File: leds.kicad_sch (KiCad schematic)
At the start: 123 parts, among them U14 ADUM1201ARZ-RL7

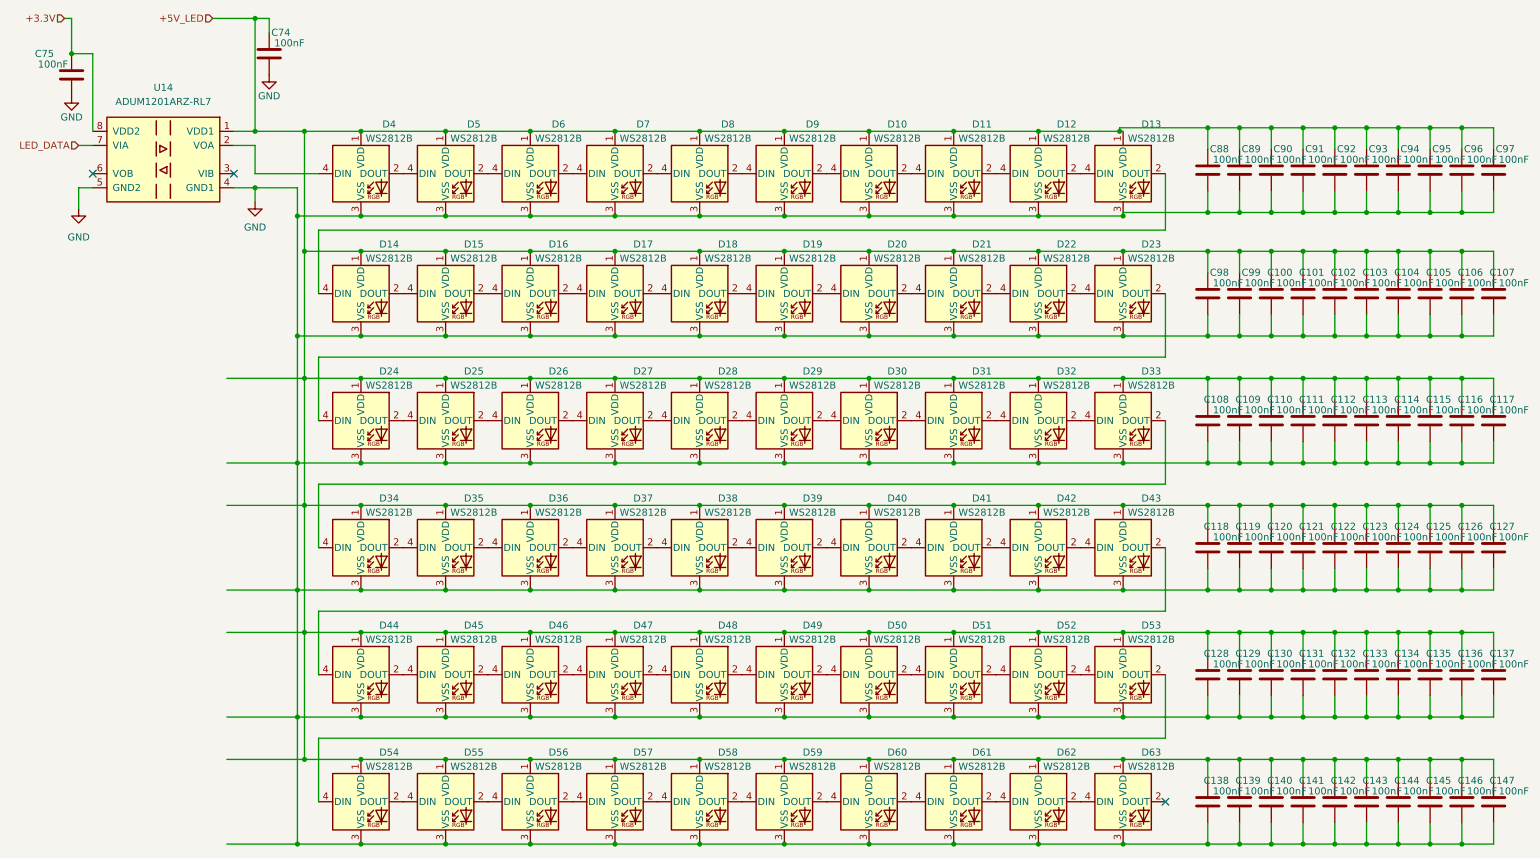
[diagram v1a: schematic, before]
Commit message: updated to kicad 9, added comparator-based power source switching
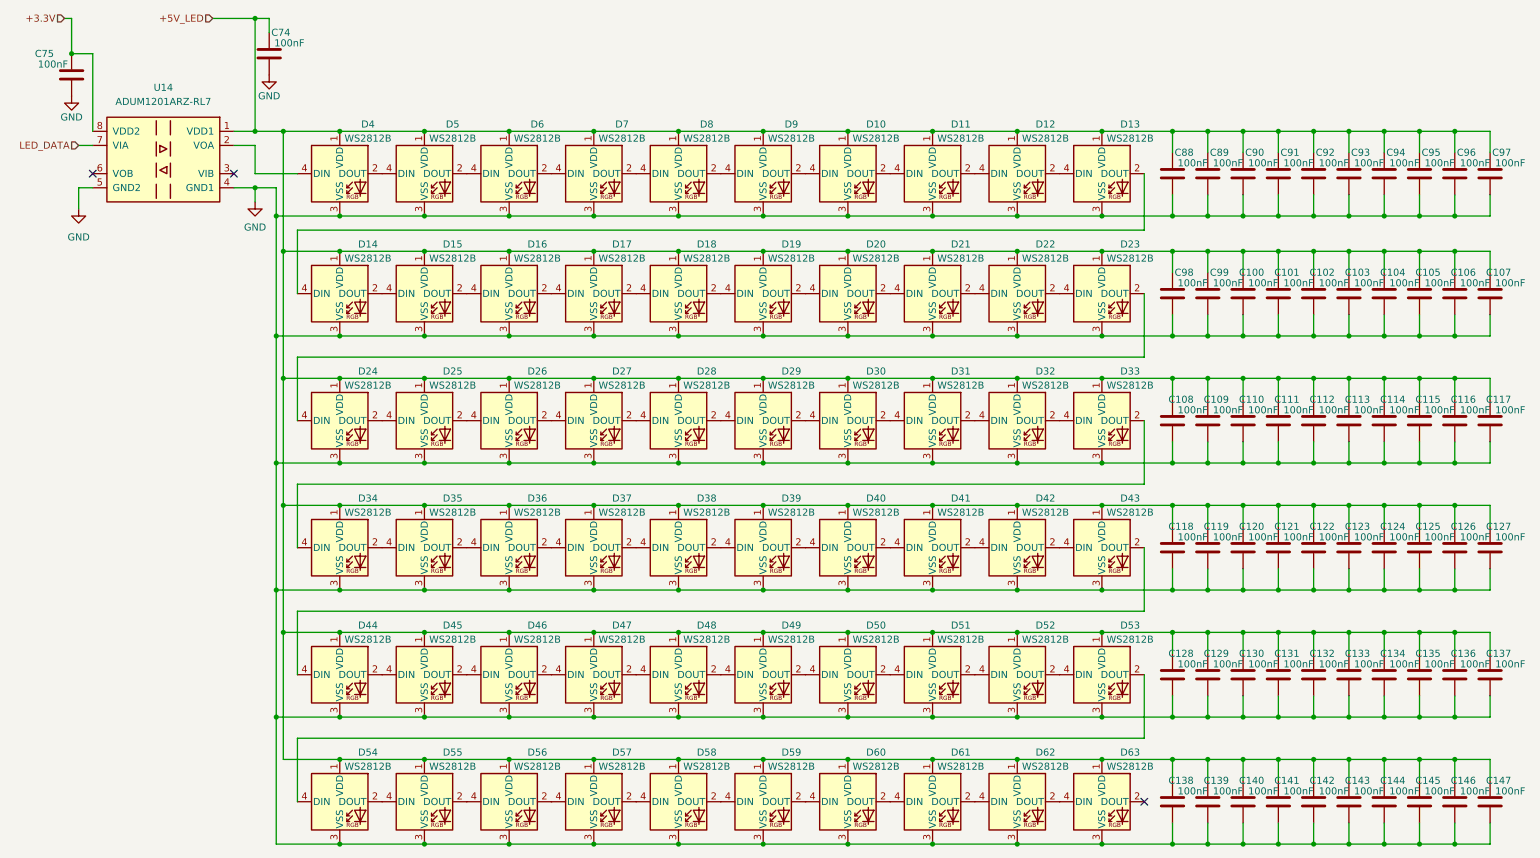
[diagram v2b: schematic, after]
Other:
- moved on the sheet: C100, C101, C102, C103, C104, C105, C106, C107, C108, C109, C110, C111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
